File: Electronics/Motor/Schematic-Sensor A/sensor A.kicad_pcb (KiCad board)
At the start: 2 copper layers, 12 x 27 mm, 3 parts, among them J1 CONN_01X06, U1 MA700

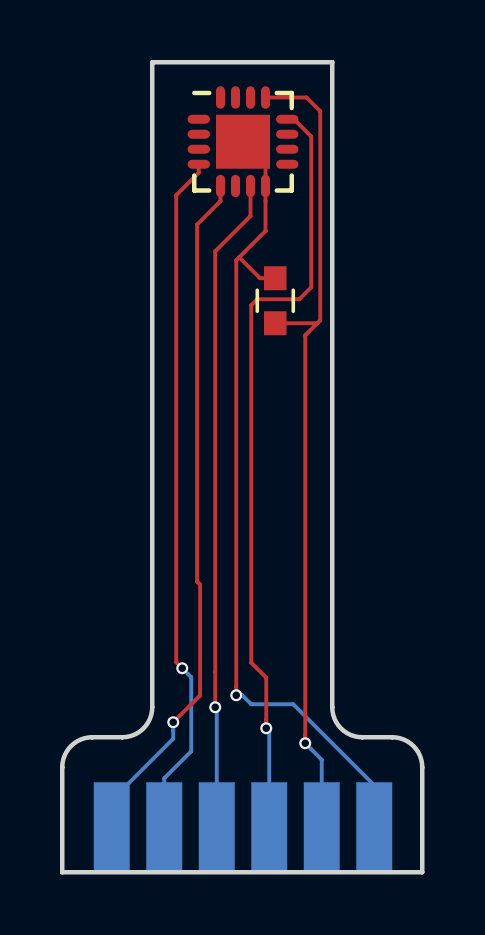
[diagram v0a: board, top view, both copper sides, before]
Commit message: motor 8 fixes; sensor flex PCB correction.
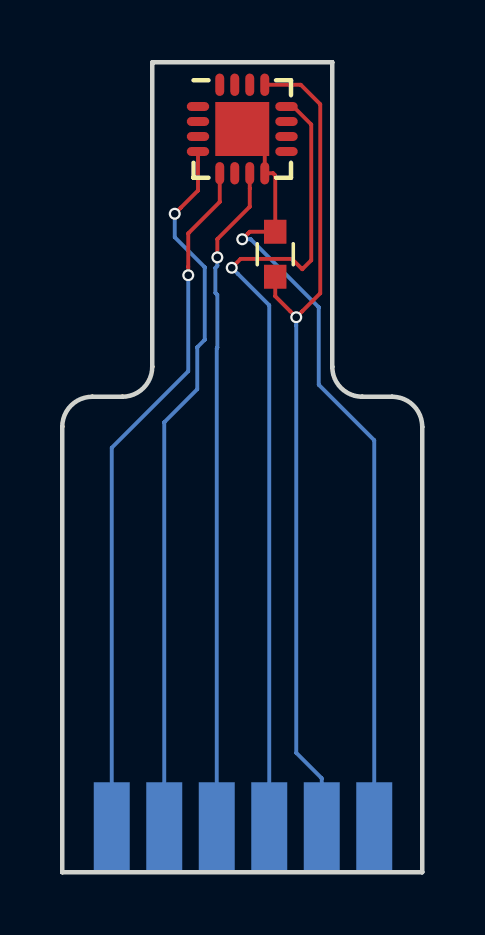
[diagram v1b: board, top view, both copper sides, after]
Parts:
- moved C1 1.55 mm to (94.1, 66.4)
- moved U1 0.43 mm to (93.0, 62.2)
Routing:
- net SCLK: track 26.0 -> 27.8 mm
- net Earth: track 30.0 -> 28.9 mm
- net MOSI: track 23.0 -> 23.8 mm
- net +3V3: track 27.7 -> 28.5 mm
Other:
- outline, holes or cut-outs redrawn

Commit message: current work
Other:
- outline, holes or cut-outs redrawn
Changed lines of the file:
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@@
     (links 12)
     (no_connects 0)
-    (area 85.336667 58.895 99.075001 89.755)
+    (area 85.336667 58.47 99.075001 89.755)
     (thickness 1.6)
     (drawings 12)
@@
     (pad_to_mask_clearance 0.2)
     (aux_axis_origin 0 0)
-    (visible_elements 7FFFFFFF)
+    (visible_elements 7FFFEFFF)
     (pcbplotparams
       (layerselection 0x010c0_80000001)
@@
     )
   )
-  (gr_arc (start 98 72.15) (end 98 71.15) (angle 90) (layer Edge.Cuts) (width 0.15))
-  (gr_arc (start 97 70.15) (end 97 71.15) (angle 90) (layer Edge.Cuts) (width 0.15))
-  (gr_arc (start 88 72.15) (end 87 72.15) (angle 90) (layer Edge.Cuts) (width 0.15))
-  (gr_arc (start 89 70.15) (end 90 70.15) (angle 90) (layer Edge.Cuts) (width 0.15))
-  (gr_line (start 98 71.15) (end 97 71.15) (layer Edge.Cuts) (width 0.15))
-  (gr_line (start 99 87) (end 99 72.15) (layer Edge.Cuts) (width 0.15))
-  (gr_line (start 88 71.15) (end 89 71.15) (layer Edge.Cuts) (width 0.15))
-  (gr_line (start 87 87) (end 87 72.15) (layer Edge.Cuts) (width 0.15))
+  (gr_arc (start 98 72.4) (end 98 71.4) (angle 90) (layer Edge.Cuts) (width 0.15))
+  (gr_arc (start 97 70.4) (end 97 71.4) (angle 90) (layer Edge.Cuts) (width 0.15))
+  (gr_arc (start 88 72.4) (end 87 72.4) (angle 90) (layer Edge.Cuts) (width 0.15))
+  (gr_arc (start 89 70.4) (end 90 70.4) (angle 90) (layer Edge.Cuts) (width 0.15))
+  (gr_line (start 98 71.4) (end 97 71.4) (layer Edge.Cuts) (width 0.15))
+  (gr_line (start 99 87) (end 99 72.4) (layer Edge.Cuts) (width 0.15))
+  (gr_line (start 88 71.4) (end 89 71.4) (layer Edge.Cuts) (width 0.15))
+  (gr_line (start 87 87) (end 87 72.4) (layer Edge.Cuts) (width 0.15))
   (gr_line (start 87 87) (end 99 87) (layer Edge.Cuts) (width 0.15))
   (gr_line (start 90 60) (end 96 60) (layer Edge.Cuts) (width 0.15))
-  (gr_line (start 96 60) (end 96 70.15) (layer Edge.Cuts) (width 0.15))
-  (gr_line (start 90 60) (end 90 70.15) (layer Edge.Cuts) (width 0.15))
+  (gr_line (start 96 60) (end 96 70.4) (layer Edge.Cuts) (width 0.15))
+  (gr_line (start 90 60) (end 90 70.4) (layer Edge.Cuts) (width 0.15))
   (segment (start 94.999999 68.300001) (end 94.8 68.5) (width 0.13) (layer F.Cu) (net 1))
   (segment (start 95.6 61.4) (end 95.6 67.7) (width 0.13) (layer F.Cu) (net 1))
@@
   (segment (start 94.8 83.02) (end 94.8 68.782842) (width 0.13) (layer B.Cu) (net 1))
   (via (at 94.8 68.5) (size 0.4) (drill 0.25) (layers F.Cu B.Cu) (net 1))
-  (segment (start 97.4 72.6) (end 95.55 70.75) (width 0.13) (layer B.Cu) (net 2))
-  (segment (start 97.4 85.5) (end 97.4 72.6) (width 0.13) (layer B.Cu) (net 2))
-  (segment (start 95.55 70.75) (end 95.55 68.167164) (width 0.13) (layer B.Cu) (net 2))
+  (segment (start 97.4 85.5) (end 97.4 73) (width 0.13) (layer B.Cu) (net 2))
+  (segment (start 97.4 73) (end 95.55 71.15) (width 0.13) (layer B.Cu) (net 2))
+  (segment (start 95.55 71.15) (end 95.55 68.167164) (width 0.13) (layer B.Cu) (net 2))
   (segment (start 95.55 68.167164) (end 93.282842 65.900006) (width 0.13) (layer B.Cu) (net 2))
   (segment (start 93.282842 65.900006) (end 93 65.900006) (width 0.13) (layer B.Cu) (net 2))
@@
   (segment (start 94.1 63.77) (end 94.03 63.7) (width 0.13) (layer F.Cu) (net 2))
   (segment (start 94.03 63.7) (end 93.75 63.7) (width 0.13) (layer F.Cu) (net 2))
-  (segment (start 91.2 67.1) (end 91.2 70.3) (width 0.13) (layer B.Cu) (net 3))
-  (segment (start 91.2 70.3) (end 88.65 72.85) (width 0.13) (layer B.Cu) (net 3))
-  (segment (start 88.65 72.85) (end 88.65 85.5) (width 0.13) (layer B.Cu) (net 3))
+  (segment (start 91.2 67.1) (end 91.2 70.55) (width 0.13) (layer B.Cu) (net 3))
+  (segment (start 91.2 70.55) (end 88.65 73.1) (width 0.13) (layer B.Cu) (net 3))
+  (segment (start 88.65 73.1) (end 88.65 85.5) (width 0.13) (layer B.Cu) (net 3))
   (segment (start 91.2 66.817158) (end 91.2 67.1) (width 0.13) (layer F.Cu) (net 3))
   (segment (start 91.2 65.705) (end 91.2 66.817158) (width 0.13) (layer F.Cu) (net 3))
@@
   (segment (start 90.75 65.832842) (end 91.75 66.832842) (width 0.13) (layer B.Cu) (net 4))
   (segment (start 91.75 66.832842) (end 91.75 69.25) (width 0.13) (layer B.Cu) (net 4))
-  (segment (start 91.75 69.25) (end 91.5 69.5) (width 0.13) (layer B.Cu) (net 4))
-  (segment (start 91.5 69.5) (end 91.5 70.9) (width 0.13) (layer B.Cu) (net 4))
-  (segment (start 91.5 70.9) (end 90.4 72) (width 0.13) (layer B.Cu) (net 4))
-  (segment (start 90.4 72) (end 90.4 85.5) (width 0.13) (layer B.Cu) (net 4))
+  (segment (start 91.75 69.25) (end 91.6 69.4) (width 0.13) (layer B.Cu) (net 4))
+  (segment (start 91.6 69.4) (end 91.6 71.25) (width 0.13) (layer B.Cu) (net 4))
+  (segment (start 91.6 71.25) (end 90.4 72.45) (width 0.13) (layer B.Cu) (net 4))
+  (segment (start 90.4 72.45) (end 90.4 85.5) (width 0.13) (layer B.Cu) (net 4))
   (segment (start 90.949999 64.850001) (end 90.75 65.05) (width 0.13) (layer F.Cu) (net 4))
   (segment (start 91.525 62.975) (end 91.525 64.275) (width 0.13) (layer F.Cu) (net 4))
